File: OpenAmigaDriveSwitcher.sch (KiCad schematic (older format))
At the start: 7 parts, among them J1 SWITCH, J2 SWITCH, J99 OSHW_LOGO, U1 74LS157, U8 EVEN_CIA_CHIP

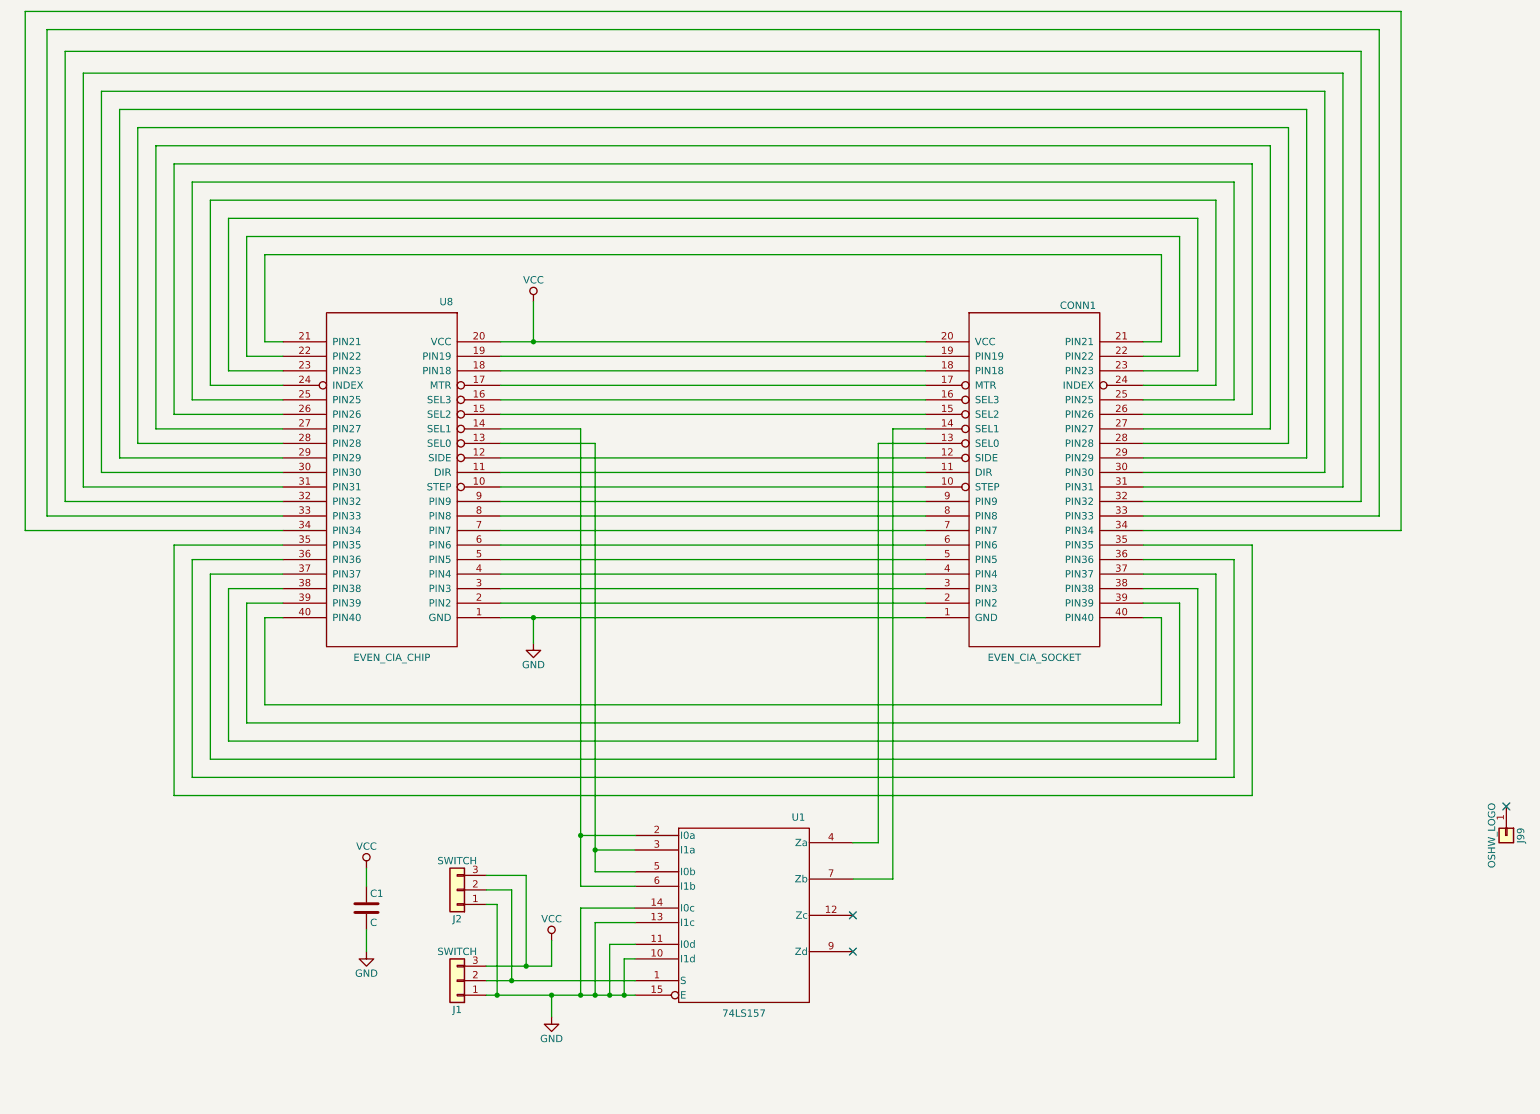
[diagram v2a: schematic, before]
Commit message: Remove legacy KiCad 4 symbols
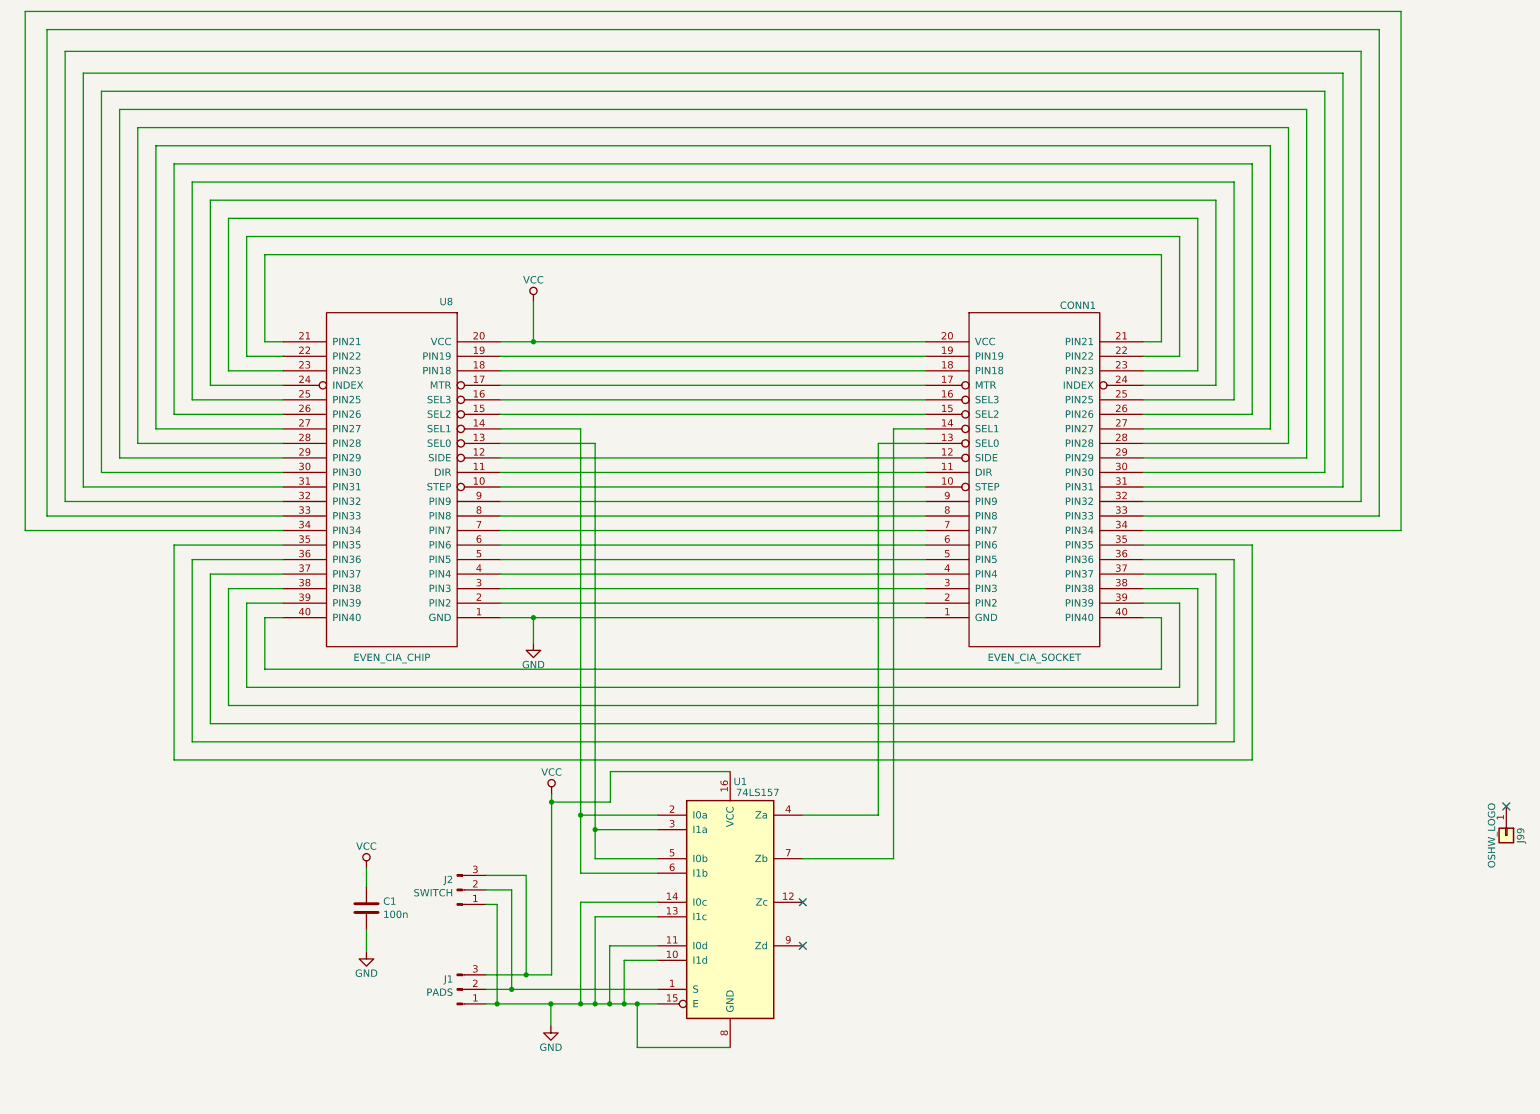
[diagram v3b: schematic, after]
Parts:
- removed C1: C, Capacitors_THT:C_Disc_D7.0mm_W2.5mm_P5.00mm, symbol OpenAmigaDriveSwitcher-rescue:C
- removed J1: SWITCH, OpenAmigaDriveSwitcher:Pin_Header_Straight_1x03-ModSilkS, symbol OpenAmigaDriveSwitcher-rescue:Conn_01x03
- removed J2: SWITCH, OpenAmigaDriveSwitcher:SolderJumper3, symbol OpenAmigaDriveSwitcher-rescue:Conn_01x03
- removed U1: 74LS157, Housings_DIP:DIP-16_W7.62mm, symbol OpenAmigaDriveSwitcher-rescue:74LS157
- added C1: 100n, Capacitor_THT:C_Disc_D7.0mm_W2.5mm_P5.00mm, symbol Device:C
- added J1: PADS, OpenAmigaDriveSwitcher:SolderJumper3, symbol Connector:Conn_01x03_Male
- added J2: SWITCH, OpenAmigaDriveSwitcher:Pin_Header_Straight_1x03-ModSilkS, symbol Connector:Conn_01x03_Male
- added U1: 74LS157, Package_DIP:DIP-16_W7.62mm, symbol 74xx:74LS157
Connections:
- net GND: now also C1.2, J1.1 (Pin_1), J2.1 (Pin_1), U1.10 (I1d), U1.11 (I0d), U1.13 (I1c), U1.14 (I0c), U1.15 (E), U1.8 (GND)
- net VCC: now also C1.1, J1.3 (Pin_3), J2.3 (Pin_3), U1.16 (VCC)
- net at U8.13 (SEL0): now also U1.3 (I1a), U1.5 (I0b)
- net at U8.14 (SEL1): now also U1.2 (I0a), U1.6 (I1b)
- net at CONN1.13 (SEL0): now also U1.4 (Za)
- net at CONN1.14 (SEL1): now also U1.7 (Zb)
- new net: J1.2 (Pin_2), J2.2 (Pin_2), U1.1 (S)
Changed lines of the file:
@@
 	1    0    0    1
 $EndComp
-$Comp
-L OpenAmigaDriveSwitcher-rescue:74LS157 U1
-U 1 1 5B315560
-P 5775 6800
-F 0 "U1" H 6150 7475 50  0000 C CNN
-F 1 "74LS157" H 5775 6125 50  0000 C CNN
-F 2 "Housings_DIP:DIP-16_W7.62mm" H 5775 6800 50  0001 C CNN
-F 3 "" H 5775 6800 50  0001 C CNN
-	1    5775 6800
-	1    0    0    -1
-$EndComp
-NoConn ~ 6525 6800
-NoConn ~ 6525 7050
+NoConn ~ 6180 6710
+NoConn ~ 6180 7010
 $Comp
 L power:GND #PWR01
 U 1 1 5B3157DD
-P 4450 7500
-F 0 "#PWR01" H 4450 7250 50  0001 C CNN
-F 1 "GND" H 4450 7350 50  0000 C CNN
-F 2 "" H 4450 7500 50  0001 C CNN
-F 3 "" H 4450 7500 50  0001 C CNN
-	1    4450 7500
+P 4445 7560
+F 0 "#PWR01" H 4445 7310 50  0001 C CNN
+F 1 "GND" H 4445 7410 50  0000 C CNN
+F 2 "" H 4445 7560 50  0001 C CNN
+F 3 "" H 4445 7560 50  0001 C CNN
+	1    4445 7560
 	1    0    0    -1
 $EndComp
@@
 	4100 4650 7025 4650
 Wire Wire Line
-	4000 7350 4075 7350
-Wire Wire Line
-	4450 7350 4450 7500
+	4000 7410 4075 7410
+Wire Wire Line
+	4445 7410 4445 7560
 Wire Wire Line
 	4325 2575 4325 2850
@@
 	4100 3450 4650 3450
 Wire Wire Line
-	6525 6300 6700 6300
-Wire Wire Line
-	6700 6300 6700 3550
+	6180 6110 6700 6110
+Wire Wire Line
+	6700 6110 6700 3550
 Wire Wire Line
 	6700 3550 7025 3550
 Wire Wire Line
-	6525 6550 6800 6550
-Wire Wire Line
-	6800 6550 6800 3450
-Wire Wire Line
-	6800 3450 7025 3450
+	6180 6410 6805 6410
+Wire Wire Line
+	6805 6410 6805 3450
+Wire Wire Line
+	6805 3450 7025 3450
 Wire Wire Line
 	2600 2850 2475 2850
@@
 	2600 4750 2475 4750
 Wire Wire Line
-	2475 4750 2475 5350
-Wire Wire Line
-	2475 5350 8650 5350
-Wire Wire Line
-	8650 5350 8650 4750
+	2475 4750 2475 5105
+Wire Wire Line
+	2475 5105 8650 5105
+Wire Wire Line
+	8650 5105 8650 4750
 Wire Wire Line
 	8650 4750 8525 4750
@@
 	8525 4650 8775 4650
 Wire Wire Line
-	8775 4650 8775 5475
-Wire Wire Line
-	8775 5475 2350 5475
-Wire Wire Line
-	2350 5475 2350 4650
+	8775 4650 8775 5230
+Wire Wire Line
+	8775 5230 2350 5230
+Wire Wire Line
+	2350 5230 2350 4650
 Wire Wire Line
 	2350 4650 2600 4650
@@
 	2600 4550 2225 4550
 Wire Wire Line
-	2225 4550 2225 5600
-Wire Wire Line
-	2225 5600 8900 5600
-Wire Wire Line
-	8900 5600 8900 4550
+	2225 4550 2225 5355
+Wire Wire Line
+	2225 5355 8900 5355
+Wire Wire Line
+	8900 5355 8900 4550
 Wire Wire Line
 	8900 4550 8525 4550
@@
 	8525 4450 9025 4450
 Wire Wire Line
-	9025 4450 9025 5725
-Wire Wire Line
-	9025 5725 2100 5725
-Wire Wire Line
-	2100 5725 2100 4450
+	9025 4450 9025 5480
+Wire Wire Line
+	9025 5480 2100 5480
+Wire Wire Line
+	2100 5480 2100 4450
 Wire Wire Line
 	2100 4450 2600 4450
@@
 	2600 4350 1975 4350
 Wire Wire Line
-	1975 4350 1975 5850
-Wire Wire Line
-	1975 5850 9150 5850
-Wire Wire Line
-	9150 5850 9150 4350
+	1975 4350 1975 5605
+Wire Wire Line
+	1975 5605 9150 5605
+Wire Wire Line
+	9150 5605 9150 4350
 Wire Wire Line
 	9150 4350 8525 4350
@@
 	8525 4250 9275 4250
 Wire Wire Line
-	9275 4250 9275 5975
-Wire Wire Line
-	9275 5975 1850 5975
-Wire Wire Line
-	1850 5975 1850 4250
+	9275 4250 9275 5730
+Wire Wire Line
+	9275 5730 1850 5730
+Wire Wire Line
+	1850 5730 1850 4250
 Wire Wire Line
 	1850 4250 2600 4250
-$Comp
-L OpenAmigaDriveSwitcher-rescue:Conn_01x03 J1
-U 1 1 5B317465
-P 3800 7250
-F 0 "J1" H 3800 7450 50  0000 C CNN
-F 1 "SWITCH" H 3800 7050 50  0000 C CNN
-F 2 "OpenAmigaDriveSwitcher:Pin_Header_Straight_1x03-ModSilkS" H 3800 7250 50  0001 C CNN
-F 3 "" H 3800 7250 50  0001 C CNN
-	1    3800 7250
-	-1   0    0    1
-$EndComp
-Wire Wire Line
-	4000 7250 4175 7250
-Connection ~ 4450 7350
-Wire Wire Line
-	4000 7150 4275 7150
-Wire Wire Line
-	4450 7150 4450 6975
+Wire Wire Line
+	4000 7310 4175 7310
+Connection ~ 4445 7410
+Wire Wire Line
+	4000 7210 4275 7210
+Wire Wire Line
+	4450 7210 4450 6020
 $Comp
 L power:VCC #PWR04
 U 1 1 5B3177E7
-P 4450 6975
-F 0 "#PWR04" H 4450 6825 50  0001 C CNN
-F 1 "VCC" H 4450 7125 50  0000 C CNN
-F 2 "" H 4450 6975 50  0001 C CNN
-F 3 "" H 4450 6975 50  0001 C CNN
-	1    4450 6975
-	1    0    0    -1
-$EndComp
-$Comp
-L OpenAmigaDriveSwitcher-rescue:C C1
-U 1 1 5B317A3C
-P 3175 6750
-F 0 "C1" H 3200 6850 50  0000 L CNN
-F 1 "C" H 3200 6650 50  0000 L CNN
-F 2 "Capacitors_THT:C_Disc_D7.0mm_W2.5mm_P5.00mm" H 3213 6600 50  0001 C CNN
-F 3 "" H 3175 6750 50  0001 C CNN
-	1    3175 6750
+P 4450 5965
+F 0 "#PWR04" H 4450 5815 50  0001 C CNN
+F 1 "VCC" H 4450 6115 50  0000 C CNN
+F 2 "" H 4450 5965 50  0001 C CNN
+F 3 "" H 4450 5965 50  0001 C CNN
+	1    4450 5965
 	1    0    0    -1
 $EndComp
@@
 NoConn ~ 11025 6050
 Wire Wire Line
-	5025 7100 4950 7100
-Wire Wire Line
-	4950 7100 4950 7350
-Connection ~ 4950 7350
-Wire Wire Line
-	5025 7000 4850 7000
-Wire Wire Line
-	4850 7000 4850 7350
-Connection ~ 4850 7350
-Wire Wire Line
-	5025 6850 4750 6850
-Wire Wire Line
-	4750 6850 4750 7350
-Connection ~ 4750 7350
-Wire Wire Line
-	5025 6750 4650 6750
-Wire Wire Line
-	4650 6750 4650 7350
-Connection ~ 4650 7350
-$Comp
-L OpenAmigaDriveSwitcher-rescue:Conn_01x03 J2
-U 1 1 5B327943
+	5180 7110 4950 7110
+Wire Wire Line
+	4950 7110 4950 7410
+Connection ~ 4950 7410
+Wire Wire Line
+	5180 7010 4850 7010
+Wire Wire Line
+	4850 7010 4850 7410
+Connection ~ 4850 7410
+Wire Wire Line
+	5180 6810 4750 6810
+Wire Wire Line
+	4750 6810 4750 7410
+Connection ~ 4750 7410
+Wire Wire Line
+	5180 6710 4650 6710
+Wire Wire Line
+	4650 6710 4650 7410
+Connection ~ 4650 7410
+Wire Wire Line
+	4000 6725 4075 6725
+Wire Wire Line
+	4075 6725 4075 7410
+Connection ~ 4075 7410
+Wire Wire Line
+	4000 6625 4175 6625
+Wire Wire Line
+	4175 6625 4175 7310
+Connection ~ 4175 7310
+Wire Wire Line
+	4000 6525 4275 6525
+Wire Wire Line
+	4275 6525 4275 7210
+Connection ~ 4275 7210
+Wire Wire Line
+	4325 2850 7025 2850
+Wire Wire Line
+	4325 4750 7025 4750
+Wire Wire Line
+	4445 7410 4650 7410
+Wire Wire Line
+	4950 7410 5040 7410
+Wire Wire Line
+	4850 7410 4950 7410
+Wire Wire Line
+	4750 7410 4850 7410
+Wire Wire Line
+	4650 7410 4750 7410
+Wire Wire Line
+	4075 7410 4445 7410
+Wire Wire Line
+	4175 7310 5180 7310
+Wire Wire Line
+	4275 7210 4450 7210
+Wire Wire Line
+	4650 6510 5180 6510
+Wire Wire Line
+	4750 6410 5180 6410
+Wire Wire Line
+	4650 3450 4650 6110
+Wire Wire Line
+	4750 3550 4750 6210
+Wire Wire Line
+	5180 6210 4750 6210
+Connection ~ 4750 6210
+Wire Wire Line
+	4750 6210 4750 6410
+Wire Wire Line
+	5180 6110 4650 6110
+Connection ~ 4650 6110
+Wire Wire Line
+	4650 6110 4650 6510
+$Comp
+L 74xx:74LS157 U1
+U 1 1 5B7F6BCD
+P 5680 6710
+F 0 "U1" H 5750 7540 50  0000 C CNN
+F 1 "74LS157" H 5870 7465 50  0000 C CNN
+F 2 "Package_DIP:DIP-16_W7.62mm" H 5680 6710 50  0001 C CNN
+F 3 "http://www.ti.com/lit/gpn/sn74LS157" H 5680 6710 50  0001 C CNN
+	1    5680 6710
+	1    0    0    -1
+$EndComp
+$Comp
+L Device:C C1
+U 1 1 5B8C4A64
+P 3175 6750
+F 0 "C1" H 3290 6796 50  0000 L CNN
+F 1 "100n" H 3290 6705 50  0000 L CNN
+F 2 "Capacitor_THT:C_Disc_D7.0mm_W2.5mm_P5.00mm" H 3213 6600 50  0001 C CNN
+F 3 "~" H 3175 6750 50  0001 C CNN
+	1    3175 6750
+	1    0    0    -1
+$EndComp
+Wire Wire Line
+	5680 7710 5040 7710
+Wire Wire Line
+	5040 7710 5040 7410
+Connection ~ 5040 7410
+Wire Wire Line
+	5040 7410 5180 7410
+Wire Wire Line
+	4450 6020 4855 6020
+Wire Wire Line
+	4855 6020 4855 5810
+Wire Wire Line
+	4855 5810 5680 5810
+Connection ~ 4450 6020
+Wire Wire Line
+	4450 6020 4450 5965
+$Comp
+L Connector:Conn_01x03_Male J2
+U 1 1 5B998C57
 P 3800 6625
-F 0 "J2" H 3800 6825 50  0000 C CNN
-F 1 "SWITCH" H 3800 6425 50  0000 C CNN
-F 2 "OpenAmigaDriveSwitcher:SolderJumper3" H 3800 6625 50  0001 C CNN
-F 3 "" H 3800 6625 50  0001 C CNN
+F 0 "J2" H 3772 6555 50  0000 R CNN
+F 1 "SWITCH" H 3772 6646 50  0000 R CNN
+F 2 "OpenAmigaDriveSwitcher:Pin_Header_Straight_1x03-ModSilkS" H 3800 6625 50  0001 C CNN
+F 3 "~" H 3800 6625 50  0001 C CNN
 	1    3800 6625
-	-1   0    0    1
-$EndComp
-Wire Wire Line
-	4000 6725 4075 6725
-Wire Wire Line
-	4075 6725 4075 7350
-Connection ~ 4075 7350
-Wire Wire Line
-	4000 6625 4175 6625
-Wire Wire Line
-	4175 6625 4175 7250
-Connection ~ 4175 7250
-Wire Wire Line
-	4000 6525 4275 6525
-Wire Wire Line
-	4275 6525 4275 7150
-Connection ~ 4275 7150
-Wire Wire Line
-	4325 2850 7025 2850
-Wire Wire Line
-	4325 4750 7025 4750
-Wire Wire Line
-	4450 7350 4650 7350
-Wire Wire Line
-	4950 7350 5025 7350
-Wire Wire Line
-	4850 7350 4950 7350
-Wire Wire Line
-	4750 7350 4850 7350
-Wire Wire Line
-	4650 7350 4750 7350
-Wire Wire Line
-	4075 7350 4450 7350
-Wire Wire Line
-	4175 7250 5025 7250
-Wire Wire Line
-	4275 7150 4450 7150
-Wire Wire Line
-	4650 6600 5025 6600
-Wire Wire Line
-	4750 6500 5025 6500
-Wire Wire Line
-	4650 3450 4650 6250
-Wire Wire Line
-	4750 3550 4750 6350
-Wire Wire Line
-	5025 6350 4750 6350
-Connection ~ 4750 6350
-Wire Wire Line
-	4750 6350 4750 6500
-Wire Wire Line
-	5025 6250 4650 6250
-Connection ~ 4650 6250
-Wire Wire Line
-	4650 6250 4650 6600
+	1    0    0    1
+$EndComp
+$Comp
+L Connector:Conn_01x03_Male J1
+U 1 1 5B9A223C
+P 3800 7310
+F 0 "J1" H 3772 7240 50  0000 R CNN
+F 1 "PADS" H 3772 7331 50  0000 R CNN
+F 2 "OpenAmigaDriveSwitcher:SolderJumper3" H 3800 7310 50  0001 C CNN
+F 3 "~" H 3800 7310 50  0001 C CNN
+	1    3800 7310
+	1    0    0    1
+$EndComp
 $EndSCHEMATC
